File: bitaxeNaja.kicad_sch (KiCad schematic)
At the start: 13 parts, among them J1 XT30

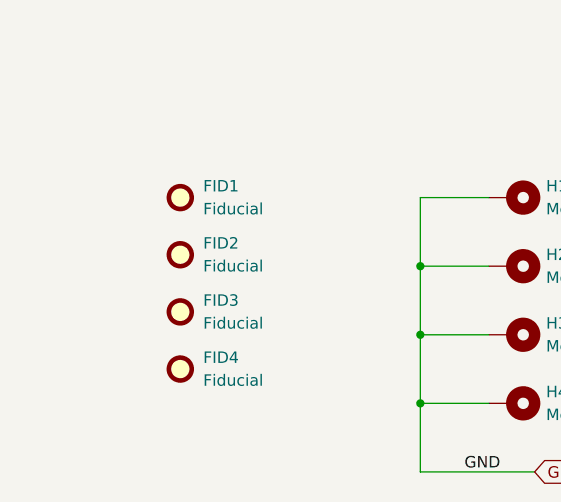
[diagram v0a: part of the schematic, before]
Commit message: placed and routed and DRC'd. updated TPS546 for 1.0V output.
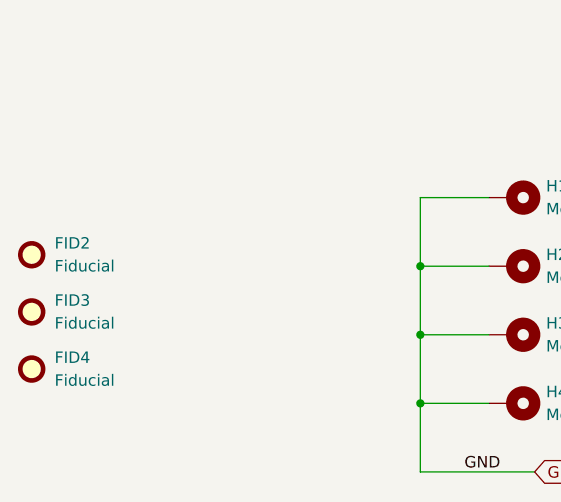
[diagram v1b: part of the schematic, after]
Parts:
- removed FID1: Fiducial, bitaxe:Fiducial_1mm_Mask2mm, symbol Mechanical:Fiducial
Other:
- moved on the sheet: FID2, FID3, FID4
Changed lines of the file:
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@@
 	(symbol
 		(lib_id "Mechanical:Fiducial")
-		(at 44.45 158.75 0)
+		(at 27.94 158.75 0)
 		(unit 1)
 		(exclude_from_sim yes)
@@
 		(fields_autoplaced yes)
 		(property "Reference" "FID2"
-			(at 46.99 157.4799 0)
+			(at 30.48 157.4799 0)
 			(effects
 				(font
@@
 		)
 		(property "Value" "Fiducial"
-			(at 46.99 160.0199 0)
+			(at 30.48 160.0199 0)
 			(effects
 				(font
@@
 		)
 		(property "Footprint" "bitaxe:Fiducial_1mm_Mask2mm"
-			(at 44.45 158.75 0)
-			(effects
-				(font
-					(size 1.27 1.27)
-				)
-				(hide yes)
-			)
-		)
-		(property "Datasheet" "~"
-			(at 44.45 158.75 0)
+			(at 27.94 158.75 0)
+			(effects
+				(font
+					(size 1.27 1.27)
+				)
+				(hide yes)
+			)
+		)
+		(property "Datasheet" "~"
+			(at 27.94 158.75 0)
 			(effects
 				(font
@@
 		)
 		(property "Description" "Fiducial Marker"
-			(at 44.45 158.75 0)
+			(at 27.94 158.75 0)
 			(effects
 				(font
@@
 	(symbol
 		(lib_id "Mechanical:Fiducial")
-		(at 44.45 171.45 0)
+		(at 27.94 171.45 0)
 		(unit 1)
 		(exclude_from_sim yes)
@@
 		(fields_autoplaced yes)
 		(property "Reference" "FID4"
-			(at 46.99 170.1799 0)
+			(at 30.48 170.1799 0)
 			(effects
 				(font
@@
 		)
 		(property "Value" "Fiducial"
-			(at 46.99 172.7199 0)
+			(at 30.48 172.7199 0)
 			(effects
 				(font
@@
 		)
 		(property "Footprint" "bitaxe:Fiducial_1mm_Mask2mm"
-			(at 44.45 171.45 0)
-			(effects
-				(font
-					(size 1.27 1.27)
-				)
-				(hide yes)
-			)
-		)
-		(property "Datasheet" "~"
-			(at 44.45 171.45 0)
+			(at 27.94 171.45 0)
+			(effects
+				(font
+					(size 1.27 1.27)
+				)
+				(hide yes)
+			)
+		)
+		(property "Datasheet" "~"
+			(at 27.94 171.45 0)
 			(effects
 				(font
@@
 		)
 		(property "Description" "Fiducial Marker"
-			(at 44.45 171.45 0)
+			(at 27.94 171.45 0)
 			(effects
 				(font
@@
 	(symbol
 		(lib_id "Mechanical:Fiducial")
-		(at 44.45 152.4 0)
-		(unit 1)
-		(exclude_from_sim yes)
-		(in_bom no)
-		(on_board yes)
-		(dnp no)
-		(fields_autoplaced yes)
-		(property "Reference" "FID1"
-			(at 46.99 151.1299 0)
+		(at 27.94 165.1 0)
+		(unit 1)
+		(exclude_from_sim yes)
+		(in_bom no)
+		(on_board yes)
+		(dnp no)
+		(fields_autoplaced yes)
+		(property "Reference" "FID3"
+			(at 30.48 163.8299 0)
 			(effects
 				(font
@@
 		)
 		(property "Value" "Fiducial"
-			(at 46.99 153.6699 0)
+			(at 30.48 166.3699 0)
 			(effects
 				(font
@@
 		)
 		(property "Footprint" "bitaxe:Fiducial_1mm_Mask2mm"
-			(at 44.45 152.4 0)
-			(effects
-				(font
-					(size 1.27 1.27)
-				)
-				(hide yes)
-			)
-		)
-		(property "Datasheet" "~"
-			(at 44.45 152.4 0)
+			(at 27.94 165.1 0)
+			(effects
+				(font
+					(size 1.27 1.27)
+				)
+				(hide yes)
+			)
+		)
+		(property "Datasheet" "~"
+			(at 27.94 165.1 0)
 			(effects
 				(font
@@
 		)
 		(property "Description" "Fiducial Marker"
-			(at 44.45 152.4 0)
-			(effects
-				(font
-					(size 1.27 1.27)
-				)
-				(hide yes)
-			)
-		)
-		(instances
-			(project ""
-				(path "/61fe8d2c-9301-4ad9-8caf-c47acfa835b0"
-					(reference "FID1")
-					(unit 1)
-				)
-			)
-		)
-	)
-	(symbol
-		(lib_id "Mechanical:Fiducial")
-		(at 44.45 165.1 0)
-		(unit 1)
-		(exclude_from_sim yes)
-		(in_bom no)
-		(on_board yes)
-		(dnp no)
-		(fields_autoplaced yes)
-		(property "Reference" "FID3"
-			(at 46.99 163.8299 0)
-			(effects
-				(font
-					(size 1.27 1.27)
-				)
-				(justify left)
-			)
-		)
-		(property "Value" "Fiducial"
-			(at 46.99 166.3699 0)
-			(effects
-				(font
-					(size 1.27 1.27)
-				)
-				(justify left)
-			)
-		)
-		(property "Footprint" "bitaxe:Fiducial_1mm_Mask2mm"
-			(at 44.45 165.1 0)
-			(effects
-				(font
-					(size 1.27 1.27)
-				)
-				(hide yes)
-			)
-		)
-		(property "Datasheet" "~"
-			(at 44.45 165.1 0)
-			(effects
-				(font
-					(size 1.27 1.27)
-				)
-				(hide yes)
-			)
-		)
-		(property "Description" "Fiducial Marker"
-			(at 44.45 165.1 0)
-			(effects
-				(font
+			(at 27.94 165.1 0)
+			(effects
+				(font

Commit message: update to KiCad 10
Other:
- company: (none) -> bitaxeorg

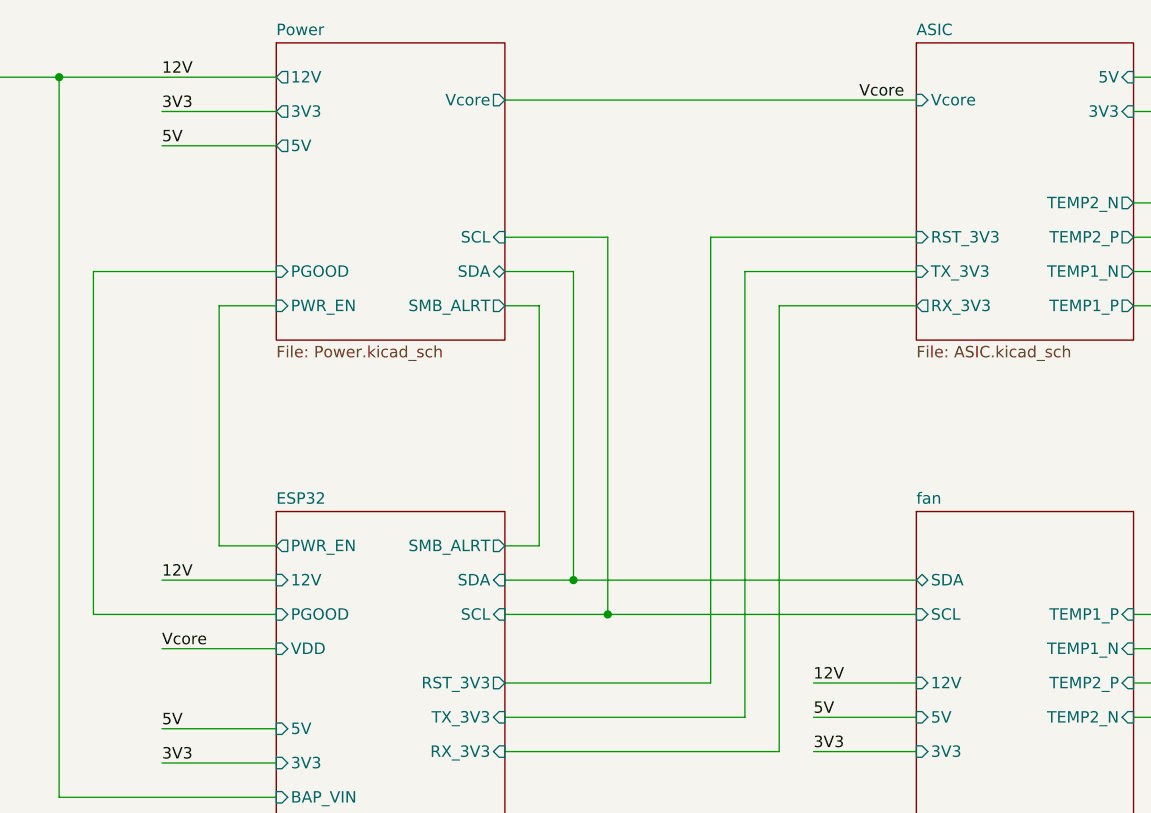
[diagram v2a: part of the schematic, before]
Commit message: switched to single phase TPS546D24 and put the ASICs in series.
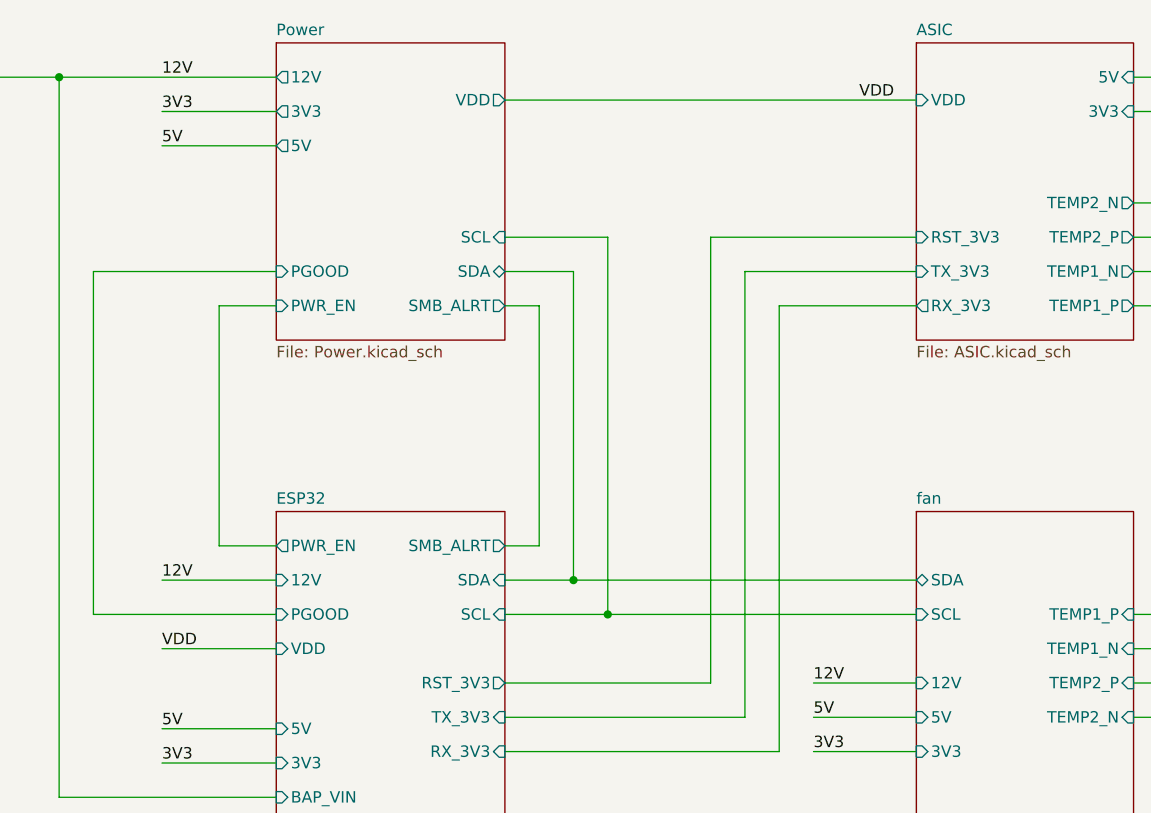
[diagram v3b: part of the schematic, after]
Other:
- sheet ASIC ports: added VDD; removed Vcore
- sheet Power ports: added VDD; removed Vcore
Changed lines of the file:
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@@
 	(title_block
 		(title "bitaxeNaja")
-		(date "2025-07-17")
-		(rev "1200x")
+		(date "2026-06-18")
+		(rev "1201x")
 		(company "bitaxeorg")
 		(comment 1 "OHL v2")
@@
 		)
 	)
-	(label "Vcore"
+	(label "VDD"
 		(at 90.17 107.95 0)
 		(effects
@@
 		)
 	)
-	(label "Vcore"
+	(label "VDD"
 		(at 167.64 46.99 0)
 		(effects
@@
 			)
 		)
-		(pin "Vcore" output
+		(pin "VDD" output
 			(at 128.27 46.99 0)
 			(effects
@@
 			)
 		)
-		(pin "Vcore" input
+		(pin "VDD" input
 			(at 173.99 46.99 180)
 			(effects

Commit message: rough parts placement.
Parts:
- removed H5, H6, H7, H8: MountingHole_Pad, bitaxe:Sinhoo SMTSO3015CTJ_nopaste, symbol Mechanical:MountingHole_Pad
- added HS1: Heatsink, bitaxe:Heatsink-5hole-BitaxeGT, symbol bitaxe:Heatsink
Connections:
- no-connect marks 0 -> 5

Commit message: finished placing parts. lots of routing.
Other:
- sheet ASIC ports: added 5V_SWITCH; removed 5V
- sheet ESP32 ports: added 5V_SWITCH; removed none
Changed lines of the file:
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@@
+	(wire
+		(pts
+			(xy 146.05 110.49) (xy 146.05 50.8)
+		)
+		(stroke
+			(width 0)
+			(type default)
+		)
+	)
 	(wire
 		(pts
@@
 	(wire
 		(pts
-			(xy 210.82 48.26) (xy 198.12 48.26)
+			(xy 198.12 46.99) (xy 210.82 46.99)
 		)
 		(stroke
@@
 	(wire
 		(pts
-			(xy 154.94 115.57) (xy 128.27 115.57)
+			(xy 154.94 120.65) (xy 128.27 120.65)
 		)
 		(stroke
@@
 	(wire
 		(pts
-			(xy 151.13 62.23) (xy 151.13 111.76)
+			(xy 151.13 62.23) (xy 151.13 116.84)
 		)
 		(stroke
@@
 	(wire
 		(pts
+			(xy 146.05 50.8) (xy 173.99 50.8)
+		)
+		(stroke
+			(width 0)
+			(type default)
+		)
+	)
+	(wire
+		(pts
 			(xy 198.12 107.95) (xy 214.63 107.95)
 		)
@@
 	(wire
 		(pts
-			(xy 158.75 69.85) (xy 158.75 119.38)
+			(xy 158.75 69.85) (xy 158.75 124.46)
 		)
 		(stroke
@@
 	(wire
 		(pts
+			(xy 128.27 110.49) (xy 146.05 110.49)
+		)
+		(stroke
+			(width 0)
+			(type default)
+		)
+	)
+	(wire
+		(pts
 			(xy 82.55 66.04) (xy 82.55 104.14)
 		)
@@
 	(wire
 		(pts
-			(xy 154.94 66.04) (xy 154.94 115.57)
+			(xy 154.94 66.04) (xy 154.94 120.65)
 		)
 		(stroke
@@
 	(wire
 		(pts
-			(xy 158.75 119.38) (xy 128.27 119.38)
+			(xy 158.75 124.46) (xy 128.27 124.46)
 		)
 		(stroke
@@
 	(wire
 		(pts
-			(xy 210.82 44.45) (xy 198.12 44.45)
-		)
-		(stroke
-			(width 0)
-			(type default)
-		)
-	)
-	(wire
-		(pts
 			(xy 58.42 48.26) (xy 62.23 48.26)
 		)
@@
 	(wire
 		(pts
-			(xy 151.13 111.76) (xy 128.27 111.76)
+			(xy 151.13 116.84) (xy 128.27 116.84)
 		)
 		(stroke
@@
 		)
 	)
-	(label "5V"
-		(at 210.82 44.45 180)
-		(effects
-			(font
-				(size 1.27 1.27)
-			)
-			(justify right bottom)
-		)
-	)
 	(label "3V3"
-		(at 210.82 48.26 180)
+		(at 210.82 46.99 180)
 		(effects
 			(font
@@
 		)
 		(pin "TX_3V3" input
-			(at 128.27 115.57 0)
+			(at 128.27 120.65 0)
 			(effects
 				(font
@@
 		)
 		(pin "RX_3V3" input
-			(at 128.27 119.38 0)
+			(at 128.27 124.46 0)
 			(effects
 				(font
@@
 		)
 		(pin "RST_3V3" output
-			(at 128.27 111.76 0)
+			(at 128.27 116.84 0)
 			(effects
 				(font
@@
 				)
 				(justify left)
+			)
+		)
+		(pin "5V_SWITCH" output
+			(at 128.27 110.49 0)
+			(effects
+				(font
+					(size 1.27 1.27)
+				)
+				(justify right)
 			)
 		)
@@
 			)
 		)
-		(pin "5V" input
-			(at 198.12 44.45 0)
-			(effects
-				(font
-					(size 1.27 1.27)
-				)
-				(justify right)
-			)
-		)
 		(pin "3V3" input
-			(at 198.12 48.26 0)
+			(at 198.12 46.99 0)
 			(effects
 				(font
@@
 			)
 		)
+		(pin "5V_SWITCH" input
+			(at 173.99 50.8 180)
+			(effects
+				(font
+					(size 1.27 1.27)
+				)
+				(justify left)
+			)
+		)

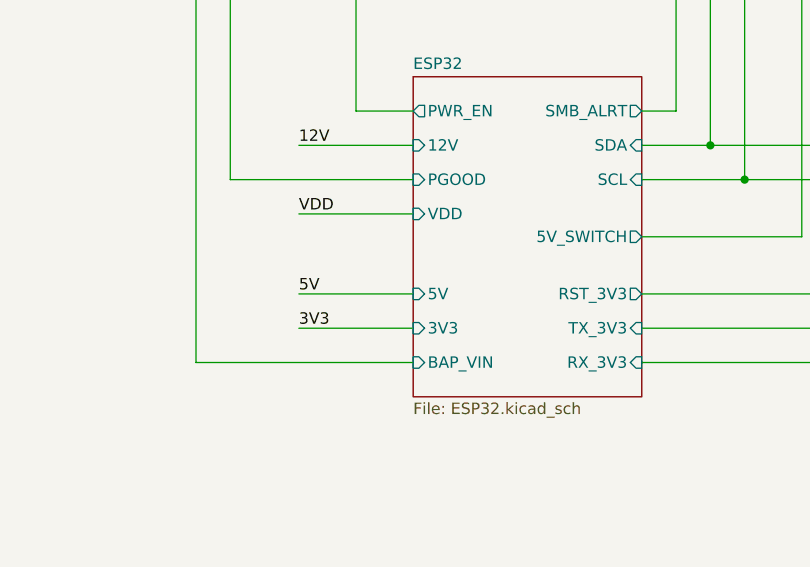
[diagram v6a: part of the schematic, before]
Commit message: fix all DRC and ERC
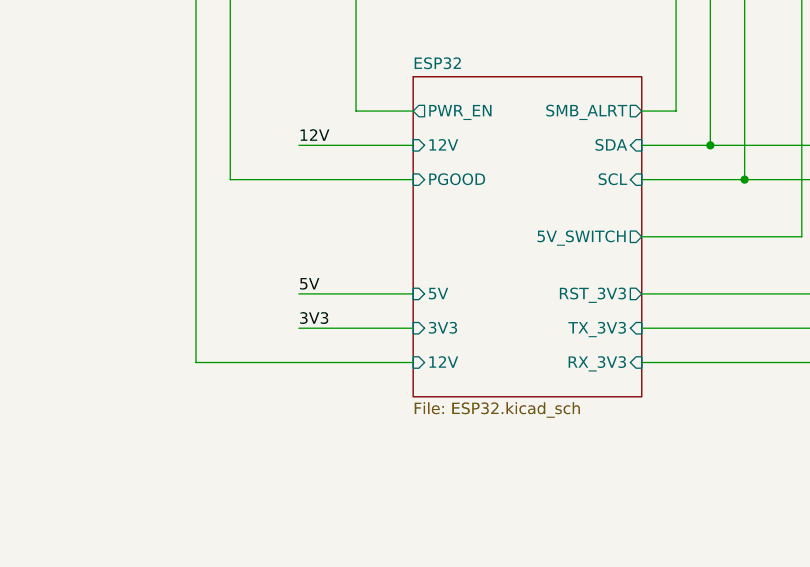
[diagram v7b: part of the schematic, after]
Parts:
- HS1: symbol bitaxe:Heatsink -> bitaxe:GTHeatsink-5hole; now in the parts list
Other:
- sheet ESP32 ports: added none; removed BAP_VIN, VDD
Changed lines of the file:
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@@
+	(wire
+		(pts
+			(xy 58.42 44.45) (xy 78.74 44.45)
+		)
+		(stroke
+			(width 0)
+			(type default)
+		)
+	)
 	(wire
 		(pts
@@
 	(wire
 		(pts
-			(xy 58.42 44.45) (xy 78.74 44.45)
-		)
-		(stroke
-			(width 0)
-			(type default)
-		)
-	)
-	(wire
-		(pts
 			(xy 90.17 116.84) (xy 102.87 116.84)
 		)
@@
 		(pts
 			(xy 58.42 48.26) (xy 62.23 48.26)
-		)
-		(stroke
-			(width 0)
-			(type default)
-		)
-	)
-	(wire
-		(pts
-			(xy 90.17 107.95) (xy 102.87 107.95)
 		)
 		(stroke
@@
 	(label "3V3"
 		(at 90.17 48.26 0)
-		(effects
-			(font
-				(size 1.27 1.27)
-			)
-			(justify left bottom)
-		)
-	)
-	(label "VDD"
-		(at 90.17 107.95 0)
 		(effects
 			(font
@@
 	)
 	(symbol
-		(lib_id "bitaxe:Heatsink")
+		(lib_id "bitaxe:GTHeatsink-5hole")
 		(at 50.8 160.02 0)
 		(unit 1)
 		(body_style 1)
 		(exclude_from_sim yes)
-		(in_bom no)
+		(in_bom yes)
 		(on_board yes)
 		(in_pos_files yes)
@@
 			)
 		)
-		(pin "VDD" input
-			(at 102.87 107.95 180)
-			(effects
-				(font
-					(size 1.27 1.27)
-				)
-				(justify left)
-			)
-		)
-		(pin "BAP_VIN" input
+		(pin "12V" input
 			(at 102.87 124.46 180)
 			(effects
